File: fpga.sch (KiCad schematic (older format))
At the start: 23 parts, among them IC1 EP4CE10F17, J1 Pinheader_2x5_TH_WALL

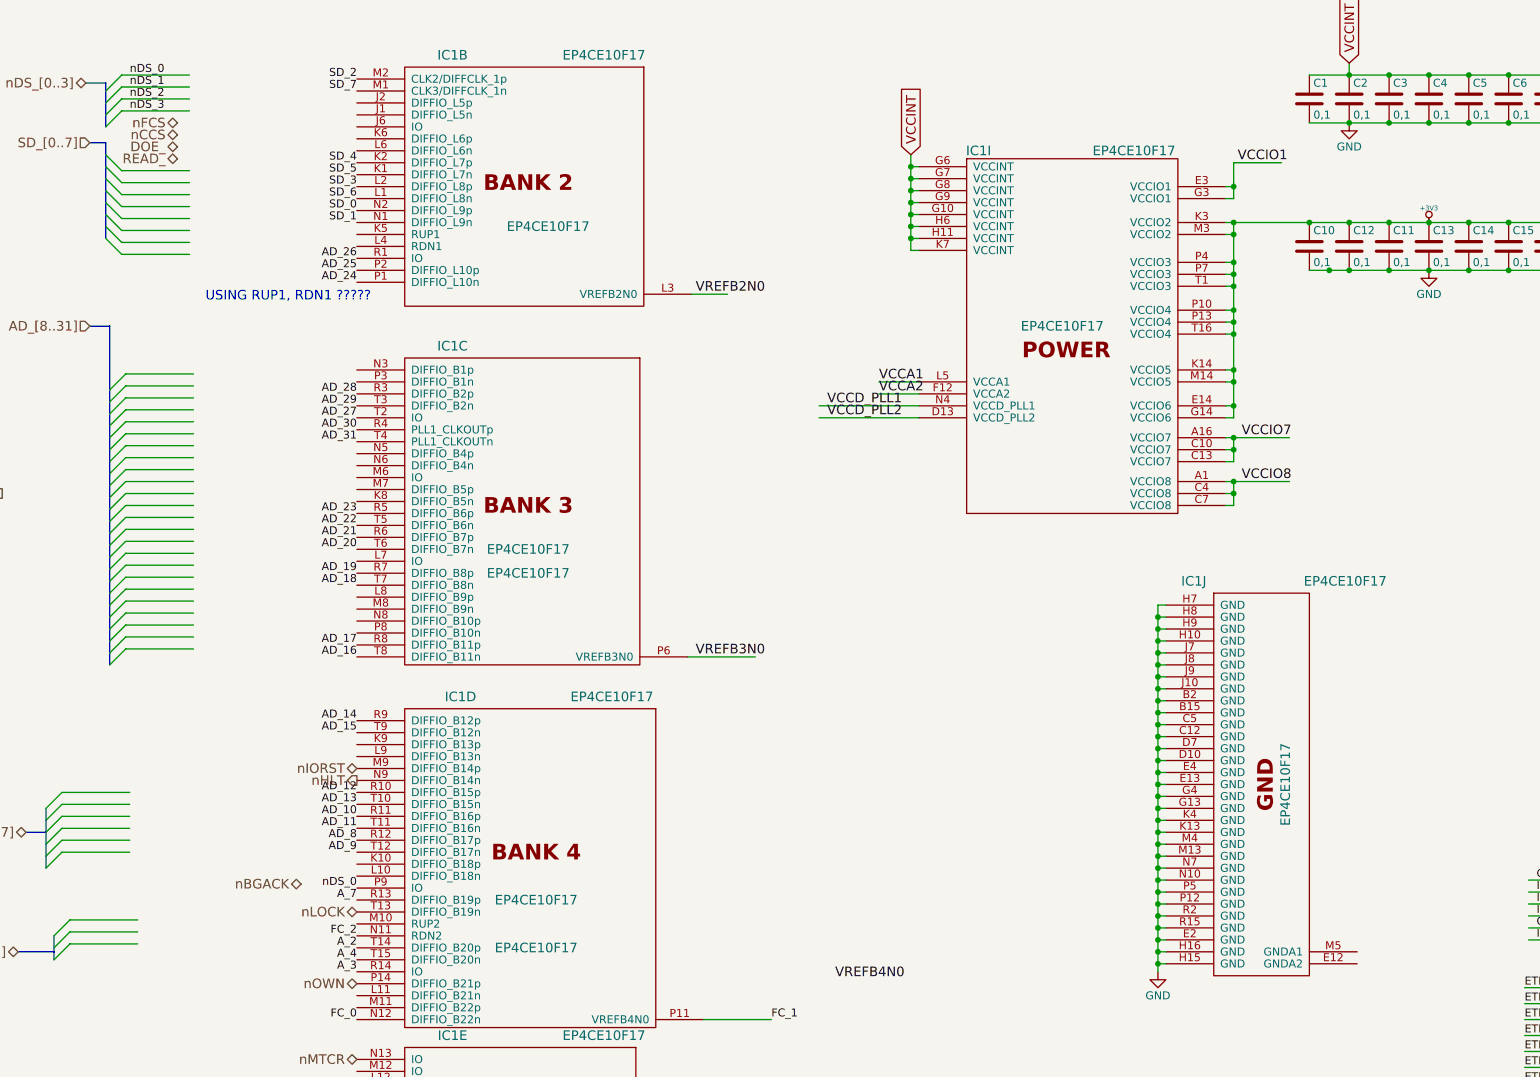
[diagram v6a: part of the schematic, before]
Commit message: Bottom PCB routing
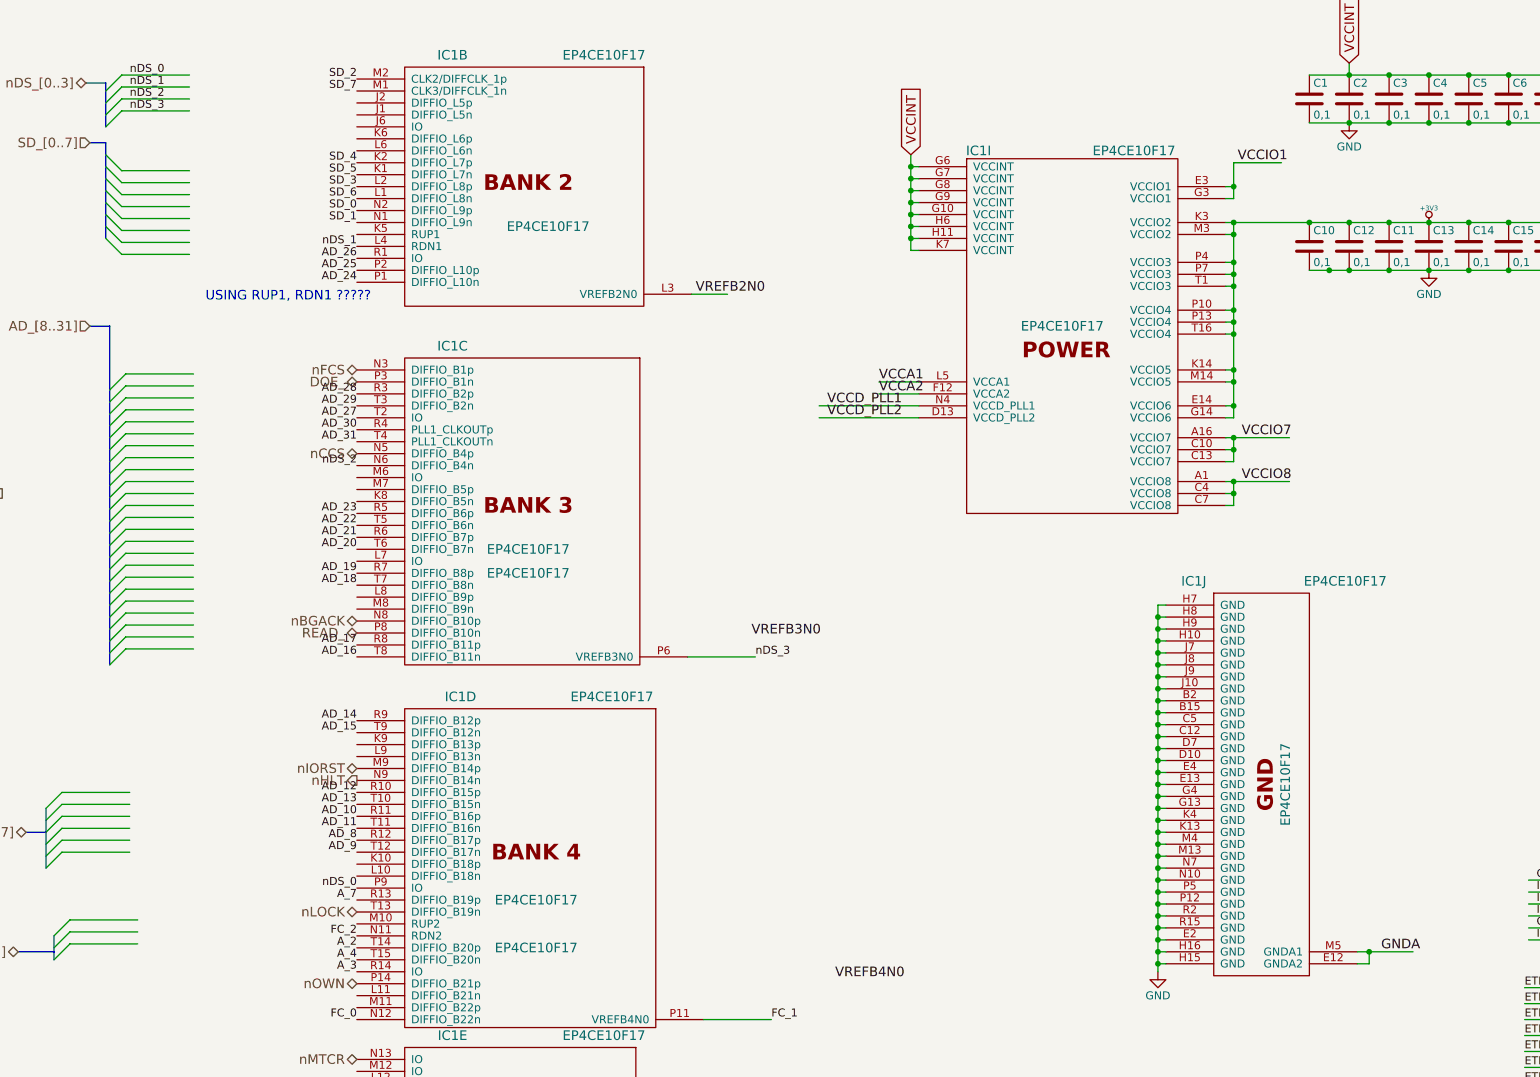
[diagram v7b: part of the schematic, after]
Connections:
- net labels added: GNDA
- wire segments 161 -> 164
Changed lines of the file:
@@
 Text HLabel 7050 6350 0    60   BiDi ~ 0
 nLOCK
-Text HLabel 5925 1400 0    60   BiDi ~ 0
+Text HLabel 7050 2950 0    60   BiDi ~ 0
 nFCS
-Text HLabel 5925 1475 0    60   BiDi ~ 0
+Text HLabel 7050 3475 0    60   BiDi ~ 0
 nCCS
-Text HLabel 5925 1550 0    60   BiDi ~ 0
+Text HLabel 7050 3025 0    60   BiDi ~ 0
 DOE_
-Text HLabel 5925 1625 0    60   BiDi ~ 0
+Text HLabel 7050 4600 0    60   BiDi ~ 0
 READ_
 Text HLabel 7050 5450 0    60   BiDi ~ 0
@@
 Text Label 10050 6775 0    60   ~ 0
 VREFB4N0
-Text Label 9175 4750 0    60   ~ 0
+Text Label 9525 4625 0    60   ~ 0
 VREFB3N0
 Text Label 9175 2475 0    60   ~ 0
@@
 	1    0    0    -1
 $EndComp
-Text HLabel 6700 6175 0    60   BiDi ~ 0
+Text HLabel 7050 4525 0    60   BiDi ~ 0
 nBGACK
 Text HLabel 7050 6800 0    60   BiDi ~ 0
@@
 Text Label 7050 6200 2    50   ~ 0
 nDS_0
+Text Label 7050 3550 2    50   ~ 0
+nDS_2
+Text Label 9550 4750 0    50   ~ 0
+nDS_3
+Wire Wire Line
+	13325 6675 13400 6675
+Wire Wire Line
+	13400 6675 13400 6600
+Wire Wire Line
+	13325 6600 13675 6600
+Connection ~ 13400 6600
+Text Label 13475 6600 0    60   ~ 0
+GNDA
+Text Label 7050 2175 2    50   ~ 0
+nDS_1
 $EndSCHEMATC
